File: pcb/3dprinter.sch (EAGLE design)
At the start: 79 parts, among them IC1 NRF51822, Q1 MOSFET, Q2 MOSFET, Q3 MOSFET, Q4 MOSFET, Y1 CRYSTAL

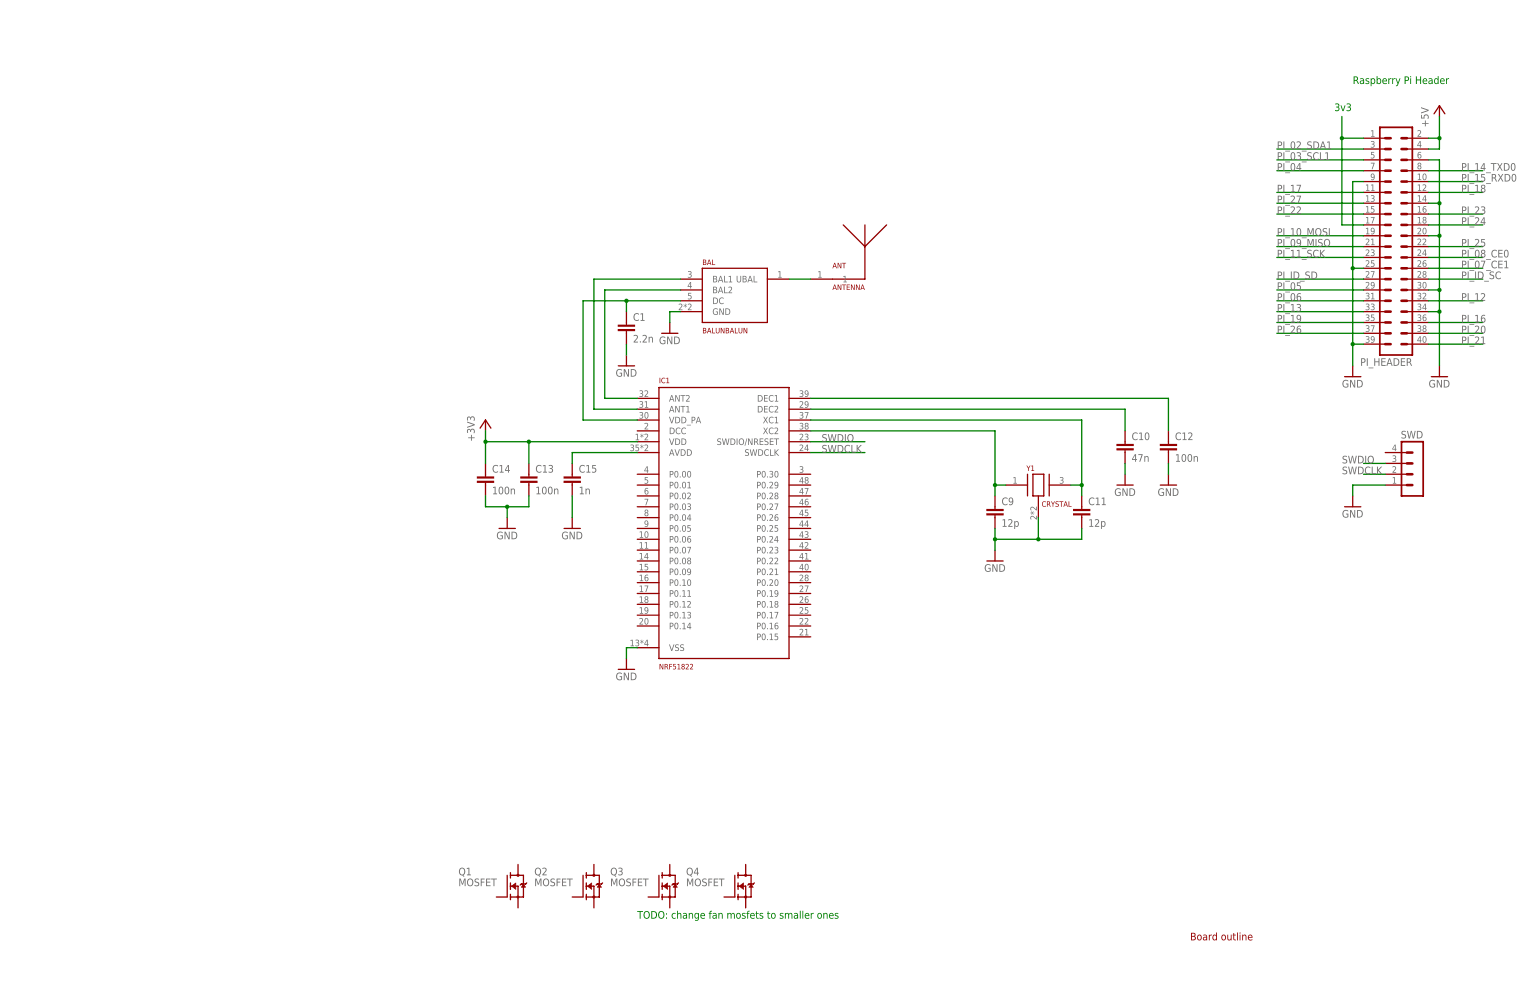
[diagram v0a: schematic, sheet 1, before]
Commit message: Added regulator and fan mosfet
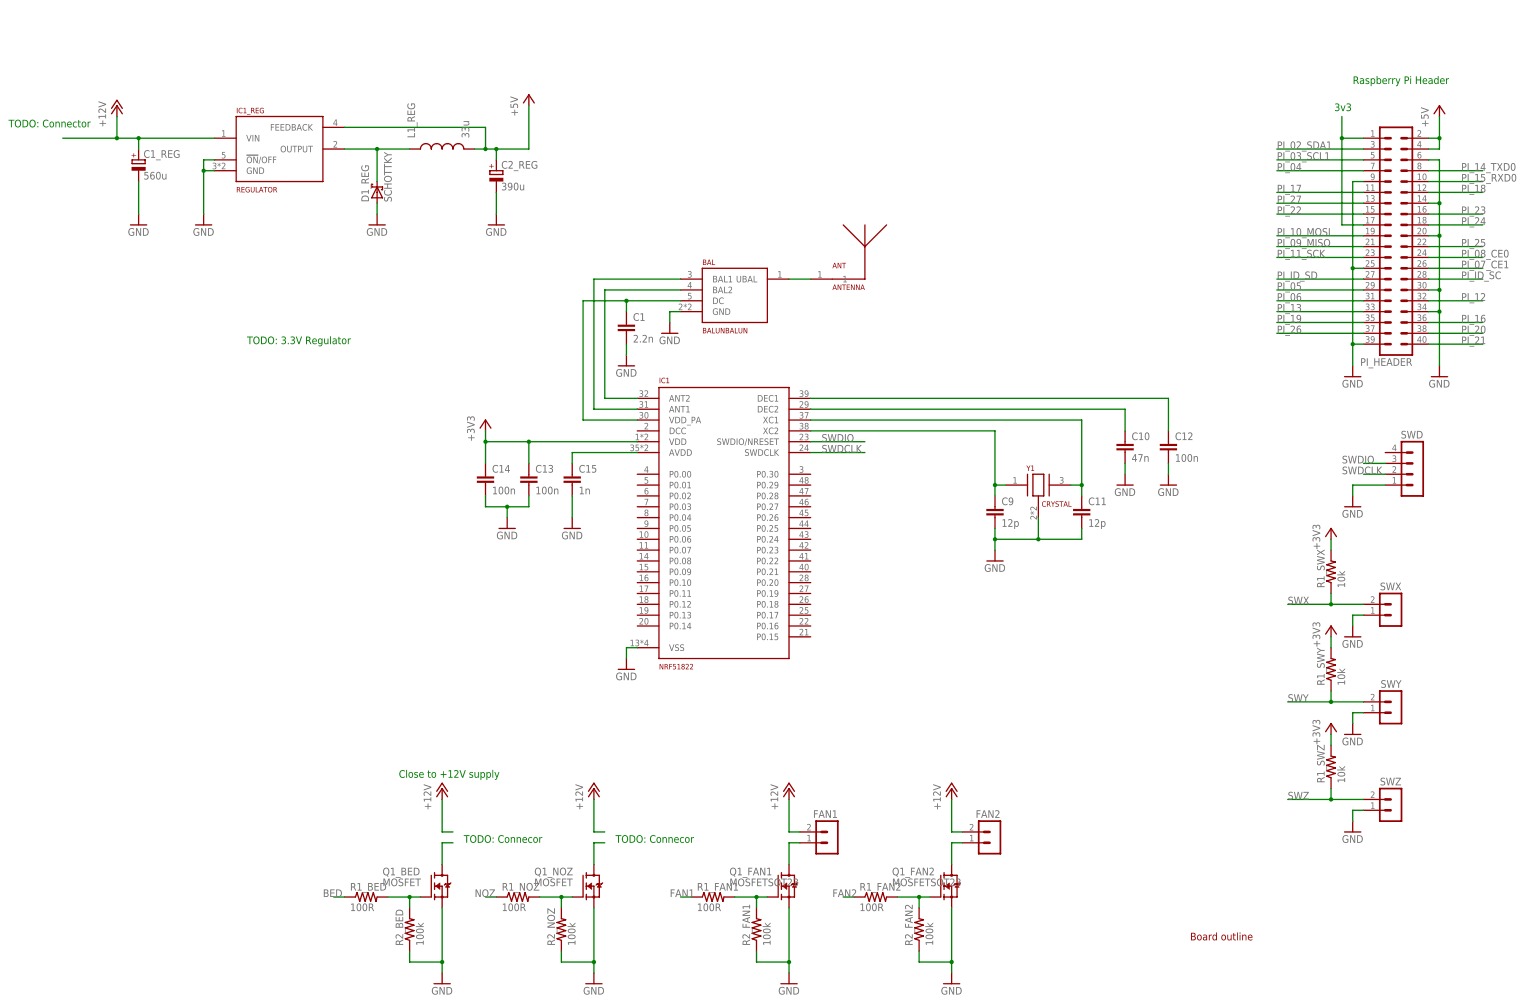
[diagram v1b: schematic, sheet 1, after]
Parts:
- removed Q1, Q3, Q4: MOSFET, 3dprinter:MOSFET
- added C1_REG: 560u, 3dprinter:TANTULUM
- added C2_REG: 390u, 3dprinter:TANTULUM
- added D1_REG: SCHOTTKY, 3dprinter:SCHOTTKY
- added FAN1, FAN2, SWX, SWY, SWZ: (no value), 3dprinter:MA02-1
- added IC1_REG: REGULATOR, 3dprinter:REGULATOR
- added L1_REG: 33u, 3dprinter:INDUCTOR
- added Q1_BED: MOSFET, 3dprinter:MOSFET
- added Q1_FAN1, Q1_FAN2: MOSFETSOT23, 3dprinter:MOSFETSOT23
- added R1_BED, R1_FAN1, R1_FAN2, R1_NOZ: 100R, 3dprinter:R-US_R0603
- added R1_SWX, R1_SWY, R1_SWZ: 10k, 3dprinter:R-US_R0603
- added R2_BED, R2_FAN1, R2_FAN2, R2_NOZ: 100k, 3dprinter:R-US_R0603
- renumbered Q2 to Q1_NOZ
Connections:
- new net BED: R1_BED.1
- new net BEDG: Q1_BED.G, R1_BED.2, R2_BED.2
- new net FAN1: R1_FAN1.1
- new net FAN1-: FAN1.1, Q1_FAN1.D
- new net FAN1G: Q1_FAN1.G, R1_FAN1.2, R2_FAN1.2
- new net FAN2: R1_FAN2.1
- new net FAN2-: FAN2.1, Q1_FAN2.D
- new net FAN2G: Q1_FAN2.G, R1_FAN2.2, R2_FAN2.2
- new net N$11: Q1_NOZ.D
- new net N$12: Q1_BED.D
- new net N$13: D1_REG.C, IC1_REG.OUTPUT, L1_REG.1
- new net NOZ: R1_NOZ.1
- new net NOZG: Q1_NOZ.G, R1_NOZ.2, R2_NOZ.2
- new net SWX: R1_SWX.1, SWX.2
- new net SWY: R1_SWY.1, SWY.2
- new net SWZ: R1_SWZ.1, SWZ.2
- net +12V: now also C1_REG.+, FAN1.2, FAN2.2, IC1_REG.VIN
- net +3V3: now also R1_SWX.2, R1_SWY.2, R1_SWZ.2
- net +5V: now also C2_REG.+, IC1_REG.FEEDBACK, L1_REG.2
- net GND: now also C1_REG.-, C2_REG.-, D1_REG.A, IC1_REG.!ON!/OFF, IC1_REG.GND, Q1_BED.S, Q1_FAN1.S, Q1_FAN2.S, Q1_NOZ.S, R2_BED.1, R2_FAN1.1, R2_FAN2.1, R2_NOZ.1, SWX.1, SWY.1, SWZ.1
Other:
- note added: "Close to +12V supply"
- note added: "TODO: 3.3V Regulator"
- note added: "TODO: Connecor"
- note added: "TODO: Connector"
- note removed: "TODO: change fan mosfets to smaller ones"

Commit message: Started component placment
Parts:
- added +12V: (no value), 3dprinter:MA04-15.08
- added BED, NOZ: (no value), 3dprinter:MA04-12.54
- added C3_REG: 1u, 3dprinter:C-EUC0805
- added C4_REG: 10n, 3dprinter:C-EUC0603
- added C5_REG: 2.2u, 3dprinter:C-EUC0805
- added IC2_REG: LP2985-3V3, 3dprinter:LP2985-3V3
- FAN1, FAN2, SWX, SWY, SWZ: device 3dprinter:MA02-1 -> 3dprinter:MA02-12.54
- MOTOR1, MOTOR2, MOTOR3, MOTOR4, SWD: device 3dprinter:MA04-1 -> 3dprinter:MA04-12.54
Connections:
- net N$1 renamed IC1_XC2
- net N$10 renamed IC1_ANT2
- net N$13 renamed IC1_REG_OUT
- net N$2 renamed IC1_XC1
- net N$3 renamed IC1_DEC1
- net N$4 renamed IC1_DEC2
- net N$5 renamed PI_3V3
- net N$6 renamed IC1_AVDD
- net N$7 renamed ANT
- net N$8 renamed IC1_VDD_PA
- net N$9 renamed IC1_ANT1
- removed net N$11: Q1_NOZ.D
- removed net N$12: Q1_BED.D
- new net BED-: BED.1, BED.2, Q1_BED.D
- new net IC2_REG_BYPASS: C4_REG.1, IC2_REG.BYPASS
- new net NOZ-: NOZ.1, NOZ.2, Q1_NOZ.D
- net +12V: now also +12V.3, +12V.4, BED.3, BED.4, C3_REG.1, IC2_REG.ON/!OFF, IC2_REG.VIN, NOZ.3, NOZ.4
- net +3V3: now also C5_REG.1, IC2_REG.VOUT
- net GND: now also +12V.1, +12V.2, C3_REG.2, C4_REG.2, C5_REG.2, IC2_REG.GND
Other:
- note added: "3V3 (Not connected to board 3V3)"
- note removed: "3v3"
- note removed: "TODO: 3.3V Regulator"
- note removed: "TODO: Connecor"
- note removed: "TODO: Connector"
- moved on the sheet: C1_REG, C2_REG, D1_REG, IC1_REG, L1_REG

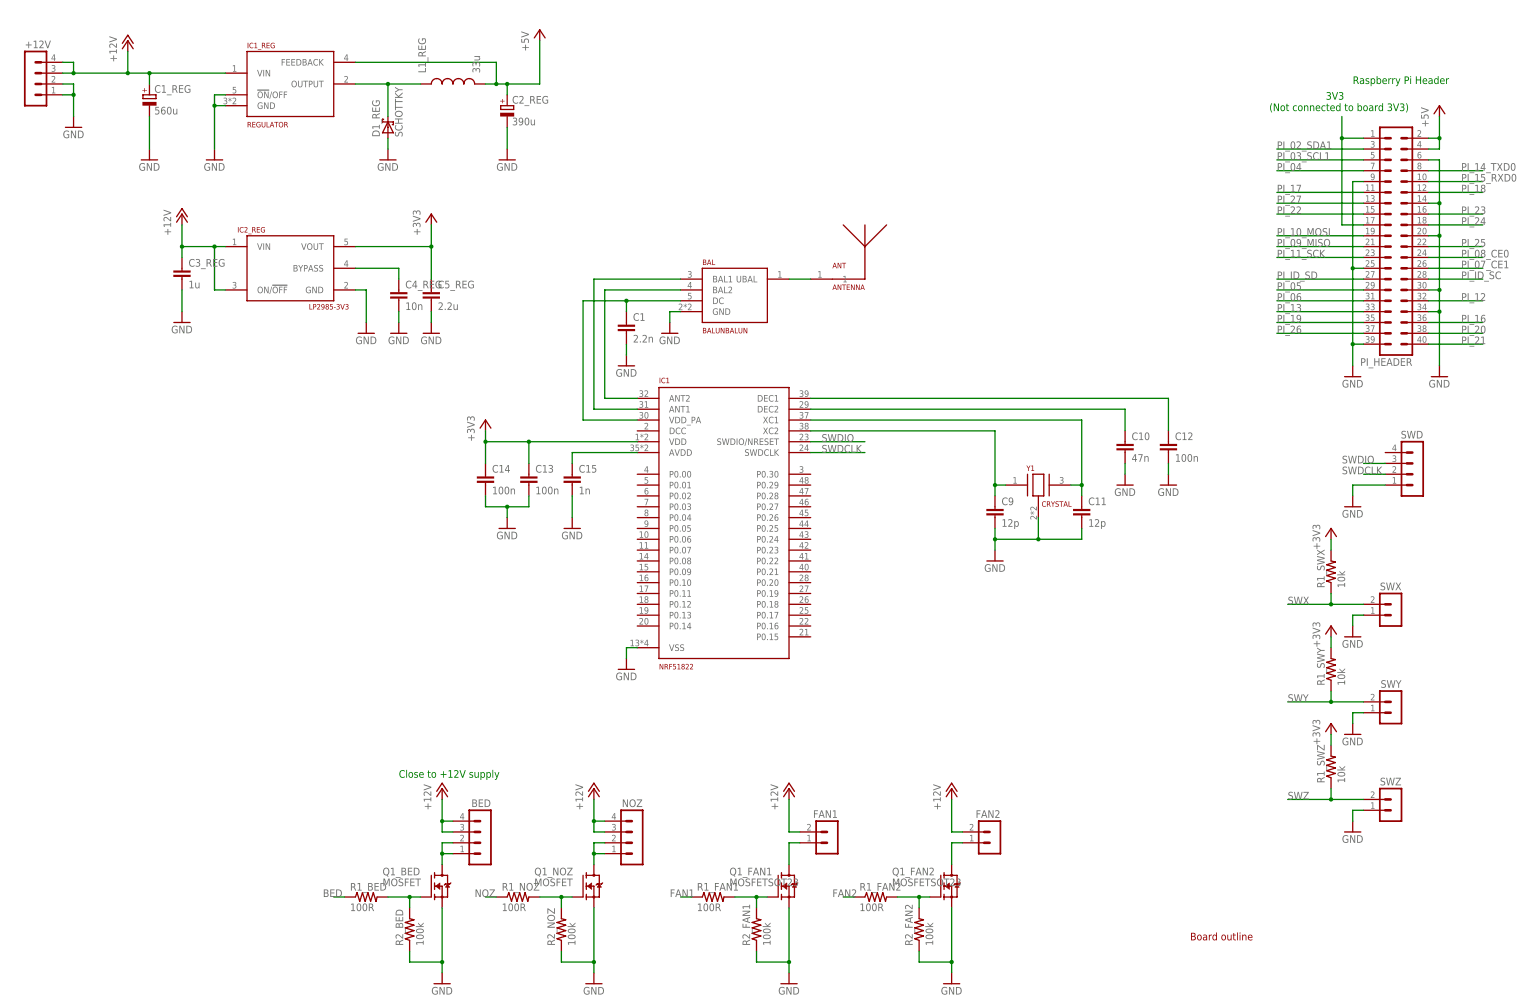
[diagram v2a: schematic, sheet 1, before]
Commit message: Rough component placement and started routing
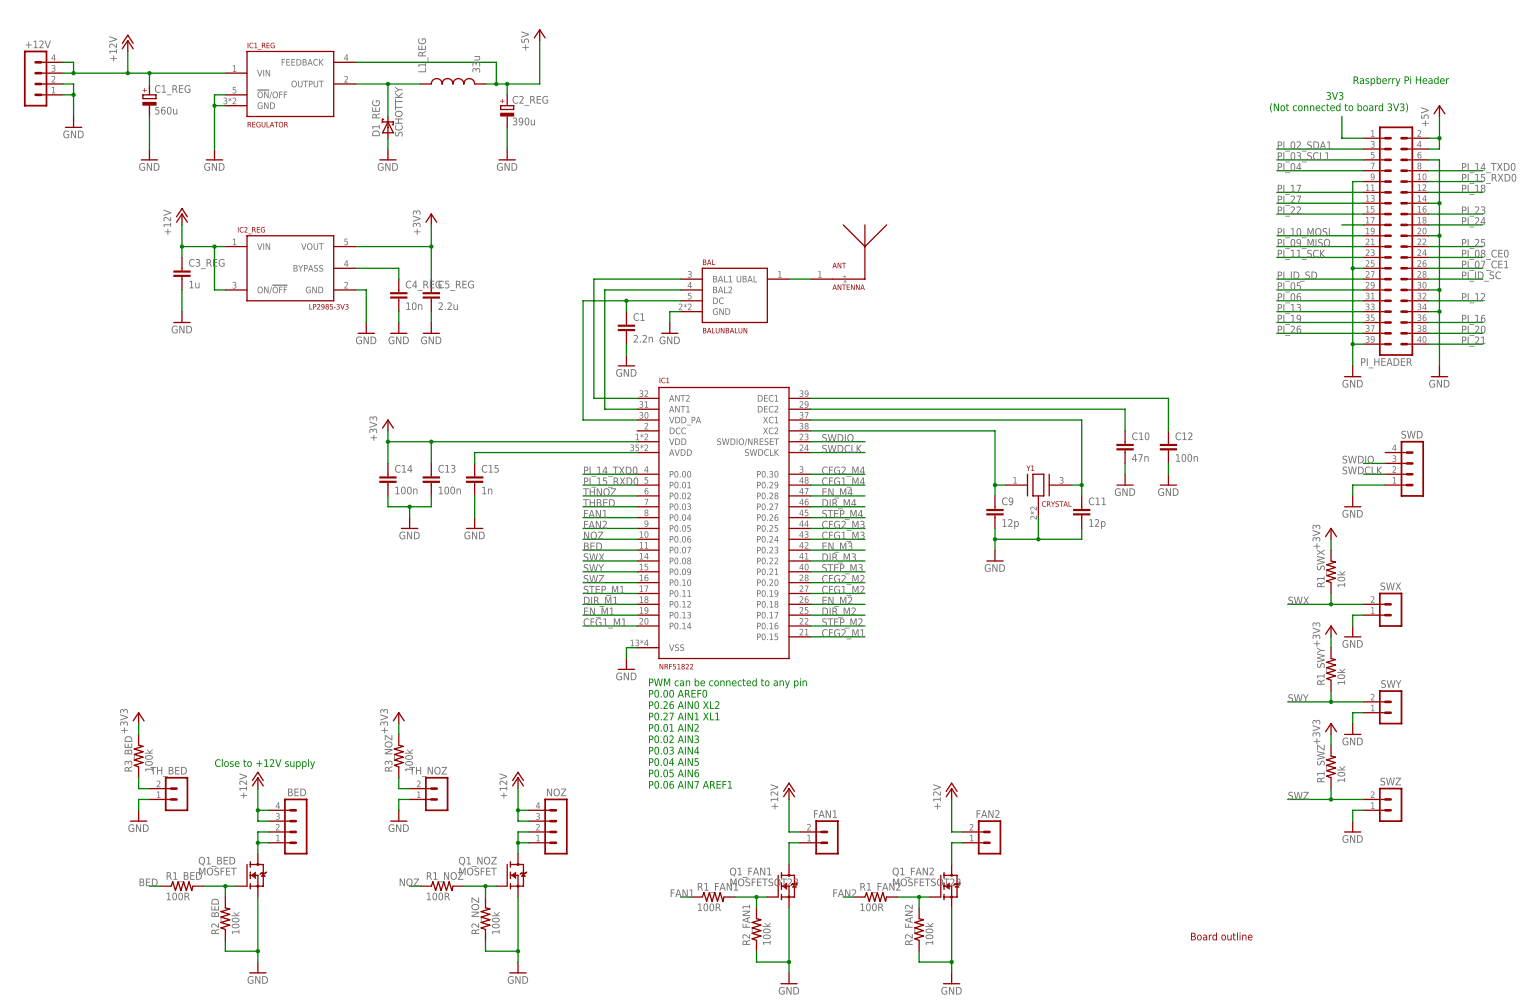
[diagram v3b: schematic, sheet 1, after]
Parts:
- added R3_BED, R3_NOZ: 100k, 3dprinter:R-US_R0603
- added TH_BED, TH_NOZ: (no value), 3dprinter:MA02-12.54
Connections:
- new net PI_3V32: PI_HEADER.17
- new net THBED: IC1.P0.03, R3_BED.1, TH_BED.2
- new net THNOZ: IC1.P0.02, R3_NOZ.1, TH_NOZ.2
- net +3V3: now also C6_M1.1, C6_M2.1, C6_M3.1, C6_M4.1, IC_M1.VCC_IO, IC_M2.VCC_IO, IC_M3.VCC_IO, IC_M4.VCC_IO, R3_BED.2, R3_NOZ.2
- net +5V: no longer C6_M1.1, C6_M2.1, C6_M3.1, C6_M4.1, IC_M1.VCC_IO, IC_M2.VCC_IO, IC_M3.VCC_IO, IC_M4.VCC_IO
- net BED: now also IC1.P0.07
- net CFG1_M1: now also IC1.P0.14
- net CFG1_M2: now also IC1.P0.19
- net CFG1_M3: now also IC1.P0.24
- net CFG1_M4: now also IC1.P0.29
- net CFG2_M1: now also IC1.P0.15
- net CFG2_M2: now also IC1.P0.20
- net CFG2_M3: now also IC1.P0.25
- net CFG2_M4: now also IC1.P0.30
- net DIR_M1: now also IC1.P0.12
- net DIR_M2: now also IC1.P0.17
- net DIR_M3: now also IC1.P0.22
- net DIR_M4: now also IC1.P0.27
- net EN_M1: now also IC1.P0.13
- net EN_M2: now also IC1.P0.18
- net EN_M3: now also IC1.P0.23
- net EN_M4: now also IC1.P0.28
- net FAN1: now also IC1.P0.04
- net FAN2: now also IC1.P0.05
- net GND: now also TH_BED.1, TH_NOZ.1
- net IC1_ANT1: now also IC1.ANT2; no longer IC1.ANT1
- net IC1_ANT2: now also IC1.ANT1; no longer IC1.ANT2
- net NOZ: now also IC1.P0.06
- net PI_14_TXD0: now also IC1.P0.00
- net PI_15_RXD0: now also IC1.P0.01
- net PI_3V3: no longer PI_HEADER.17
- net STEP_M1: now also IC1.P0.11
- net STEP_M2: now also IC1.P0.16
- net STEP_M3: now also IC1.P0.21
- net STEP_M4: now also IC1.P0.26
- net SWX: now also IC1.P0.08
- net SWY: now also IC1.P0.09
- net SWZ: now also IC1.P0.10
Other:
- note added: "PWM can be connected to any pin P0.00 AREF0 P0.26 AIN0 XL2 P0.27 AIN1 XL1 P0.01 AIN2 P0.02 AIN3 P0.03 AIN4 P0.04 AIN5 P0.05 AIN6 P0.06 AIN7 AREF1"
- moved on the sheet: BED, C13, C14, C15, NOZ, Q1_BED, Q1_NOZ, R1_BED, R1_NOZ, R2_BED, R2_NOZ

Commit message: More routing
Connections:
- net BED: now also IC1.P0.03; no longer IC1.P0.07
- net CFG1_M1: now also IC1.P0.18; no longer IC1.P0.14
- net CFG1_M2: now also IC1.P0.12; no longer IC1.P0.19
- net CFG1_M3: now also IC1.P0.25; no longer IC1.P0.24
- net CFG1_M4: now also IC1.P0.01; no longer IC1.P0.29
- net CFG2_M1: now also IC1.P0.19; no longer IC1.P0.15
- net CFG2_M2: now also IC1.P0.11; no longer IC1.P0.20
- net CFG2_M3: now also IC1.P0.24; no longer IC1.P0.25
- net CFG2_M4: now also IC1.P0.02; no longer IC1.P0.30
- net DIR_M1: now also IC1.P0.16; no longer IC1.P0.12
- net DIR_M2: now also IC1.P0.14; no longer IC1.P0.17
- net DIR_M3: now also IC1.P0.27; no longer IC1.P0.22
- net DIR_M4: now also IC1.P0.30; no longer IC1.P0.27
- net EN_M1: now also IC1.P0.20; no longer IC1.P0.13
- net EN_M2: now also IC1.P0.15; no longer IC1.P0.18
- net FAN1: now also IC1.P0.08; no longer IC1.P0.04
- net NOZ: now also IC1.P0.04; no longer IC1.P0.06
- net PI_14_TXD0: now also IC1.P0.06; no longer IC1.P0.00
- net PI_15_RXD0: now also IC1.P0.07; no longer IC1.P0.01
- net STEP_M1: now also IC1.P0.17; no longer IC1.P0.11
- net STEP_M2: now also IC1.P0.13; no longer IC1.P0.16
- net STEP_M3: now also IC1.P0.26; no longer IC1.P0.21
- net STEP_M4: now also IC1.P0.00; no longer IC1.P0.26
- net SWX: now also IC1.P0.10; no longer IC1.P0.08
- net SWY: now also IC1.P0.22; no longer IC1.P0.09
- net SWZ: now also IC1.P0.21; no longer IC1.P0.10
- net THBED: now also IC1.P0.09; no longer IC1.P0.03
- net THNOZ: now also IC1.P0.29; no longer IC1.P0.02

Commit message: More routing
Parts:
- added SJ1, SJ2, SJ3, SJ4, SJ5, SJ6, SJ7, SJ8: (no value), 3dprinter:SJ2W
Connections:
- new net P0.08: IC1.P0.08
- new net P0.09: IC1.P0.09
- new net P0.10: IC1.P0.10
- new net P0.11: IC1.P0.11
- new net P0.12: IC1.P0.12
- new net P0.13: IC1.P0.13
- new net P0.17: IC1.P0.17
- new net P0.21: IC1.P0.21
- net +3V3: now also SJ1.3, SJ2.3, SJ3.3, SJ4.3, SJ5.3, SJ6.3, SJ7.3, SJ8.3
- net BED: now also IC1.P0.05; no longer IC1.P0.03
- net CFG1_M1: now also SJ1.2; no longer IC1.P0.18
- net CFG1_M2: now also SJ3.2; no longer IC1.P0.12
- net CFG1_M3: now also SJ5.2; no longer IC1.P0.25
- net CFG1_M4: now also SJ7.2; no longer IC1.P0.01
- net CFG2_M1: now also SJ2.2; no longer IC1.P0.19
- net CFG2_M2: now also SJ4.2; no longer IC1.P0.11
- net CFG2_M3: now also SJ6.2; no longer IC1.P0.24
- net CFG2_M4: now also SJ8.2; no longer IC1.P0.02
- net DIR_M1: now also IC1.P0.19; no longer IC1.P0.16
- net DIR_M2: now also IC1.P0.15; no longer IC1.P0.14
- net DIR_M3: now also IC1.P0.23; no longer IC1.P0.27
- net DIR_M4: now also IC1.P0.27; no longer IC1.P0.30
- net EN_M2: now also IC1.P0.16; no longer IC1.P0.15
- net EN_M3: now also IC1.P0.22; no longer IC1.P0.23
- net EN_M4: now also IC1.P0.26; no longer IC1.P0.28
- net FAN1: now also IC1.P0.24; no longer IC1.P0.08
- net FAN2: now also IC1.P0.29; no longer IC1.P0.05
- net GND: now also SJ1.1, SJ2.1, SJ3.1, SJ4.1, SJ5.1, SJ6.1, SJ7.1, SJ8.1
- net STEP_M1: now also IC1.P0.18; no longer IC1.P0.17
- net STEP_M2: now also IC1.P0.14; no longer IC1.P0.13
- net STEP_M3: now also IC1.P0.25; no longer IC1.P0.26
- net STEP_M4: now also IC1.P0.28; no longer IC1.P0.00
- net SWX: now also IC1.P0.30; no longer IC1.P0.10
- net SWY: now also IC1.P0.00; no longer IC1.P0.22
- net SWZ: now also IC1.P0.01; no longer IC1.P0.21
- net THBED: now also IC1.P0.02; no longer IC1.P0.09
- net THNOZ: now also IC1.P0.03; no longer IC1.P0.29
